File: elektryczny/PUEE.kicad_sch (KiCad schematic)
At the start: 9 parts, among them U1 ESP-12, U2 LM2596S-3.3

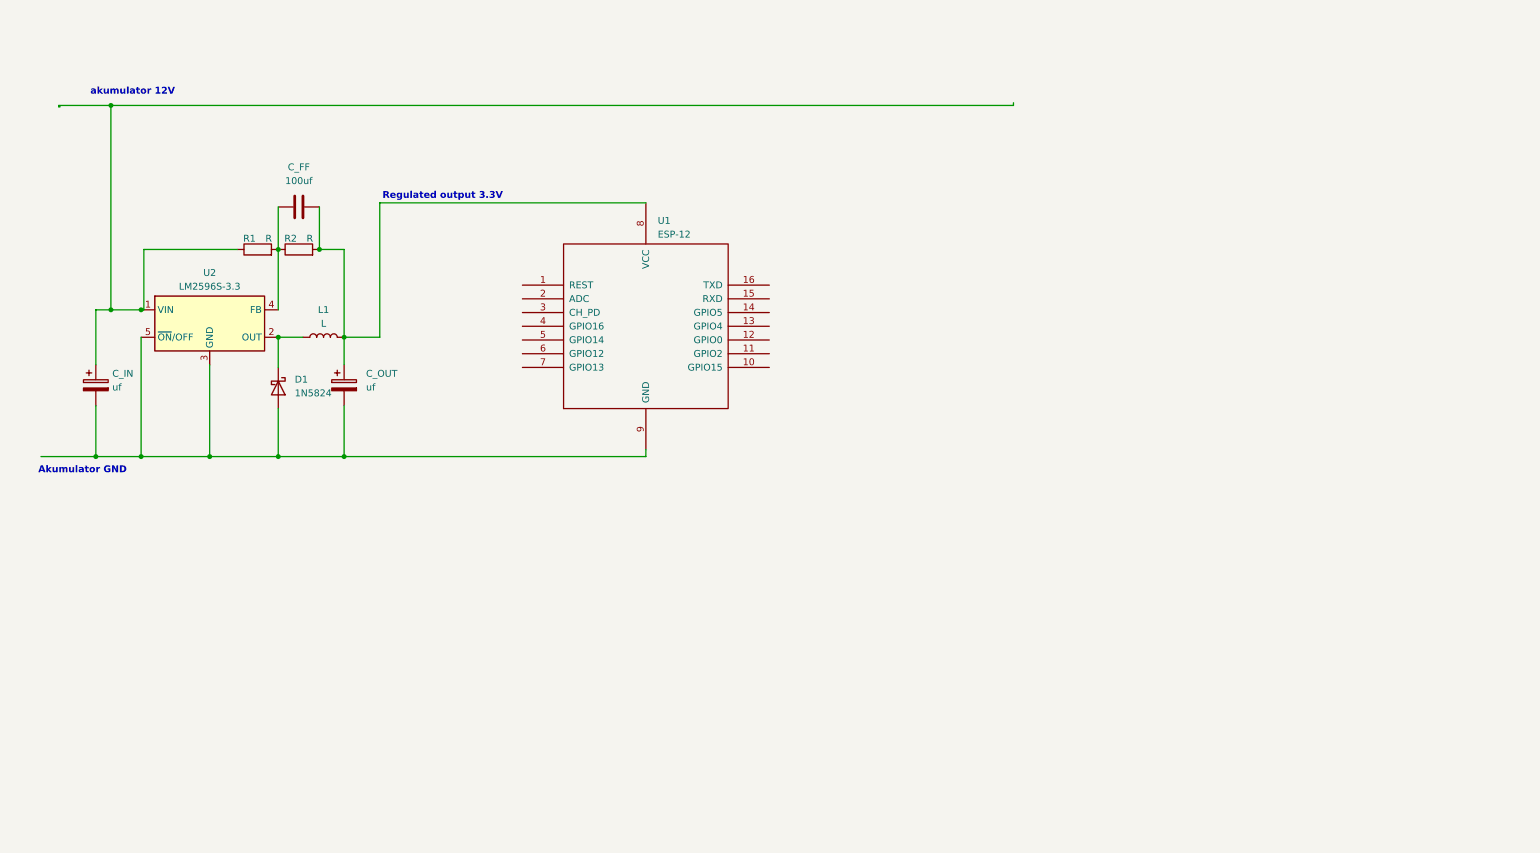
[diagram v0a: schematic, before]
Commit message: TJA1050 added
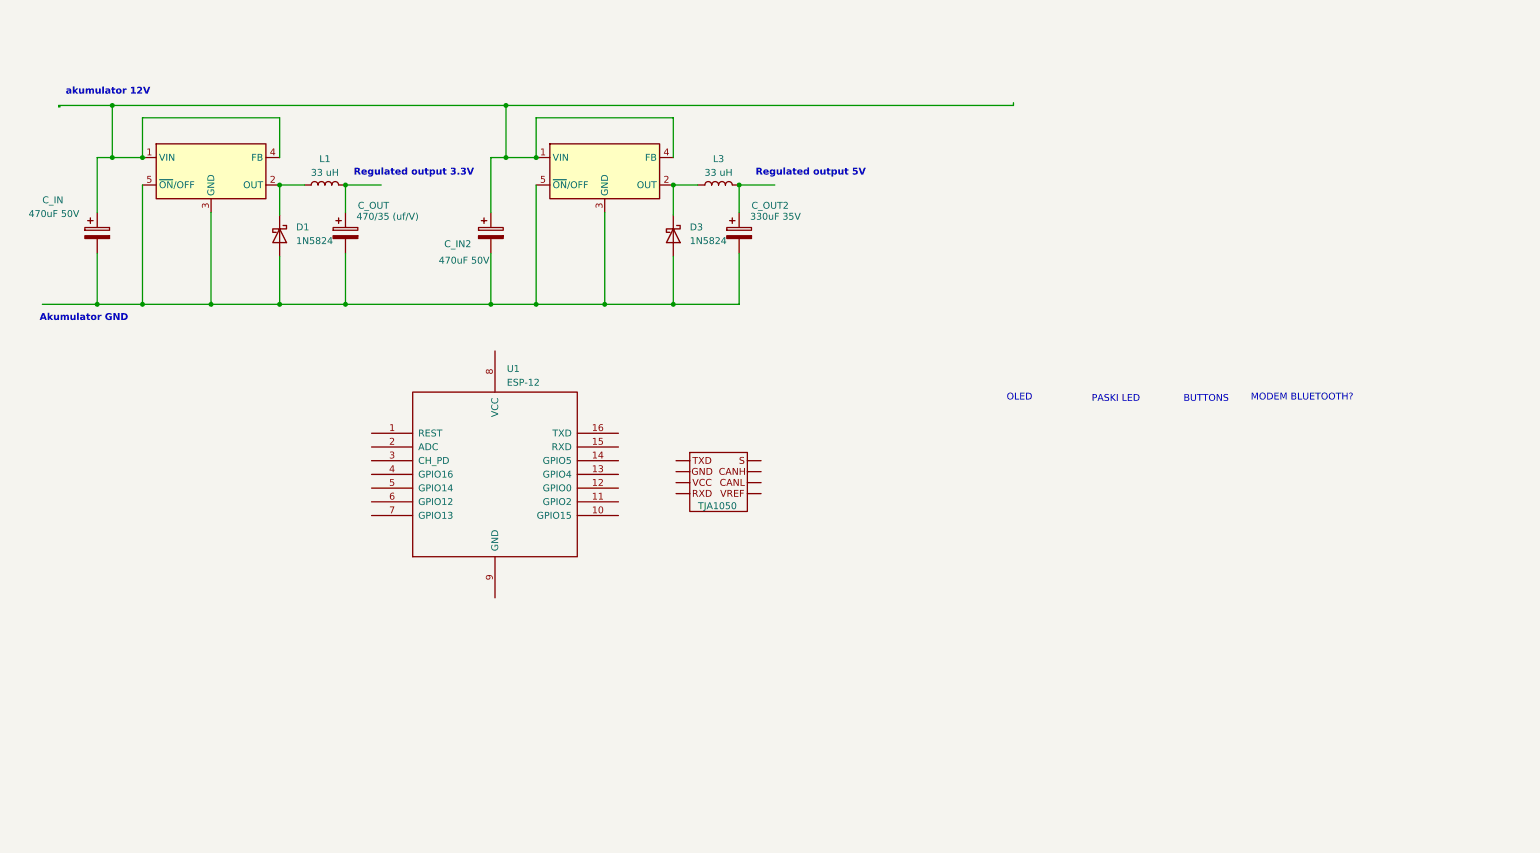
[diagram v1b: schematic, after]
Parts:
- removed C_FF: 100uf, symbol Device:C
- removed R1, R2: R, symbol Device:R
- added C_IN2: 470uF 50V, symbol Device:C_Polarized
- added C_OUT2: 330uF 35V, symbol Device:C_Polarized
- added D3: 1N5824, symbol Device:D_Schottky
- added L3: 33 uH, symbol Device:L
- added TJA1050: ~, symbol CAN:TJA1050
- added U4: LM2596, Package_TO_SOT_SMD:TO-263-5_TabPin3, symbol Regulator_Switching:LM2596S-3.3
- C_IN: value uf -> 470uF 50V
- C_OUT: value uf -> 470/35 (uf/V)
- L1: value L -> 33 uH
- U2: value LM2596S-3.3 -> LM2596
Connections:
- net at C_OUT.1, L1.2: no longer U1.8 (VCC)
- net at C_IN.2, C_OUT.2, D1.2 (A)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: now also C_IN2.2, C_OUT2.2, D3.2 (A), U4.3 (GND), U4.5 (~{ON}/OFF); no longer U1.9 (GND)
- net at U2.4 (FB): now also C_IN.1, U2.1 (VIN), C_IN2.1, U4.1 (VIN), U4.4 (FB)
- new net: D3.1 (K), L3.1, U4.2 (OUT)
- new net: C_OUT2.1, L3.2
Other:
- note added: "BUTTONS"
- note added: "MODEM BLUETOOTH?"
- note added: "OLED"
- note added: "PASKI LED"
- note added: "Regulated output 5V"
- moved on the sheet: C_IN, C_OUT, D1, L1, U1

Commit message: Wstępny schemat elektroniczny
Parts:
- removed TJA1050: ~, symbol CAN:TJA1050
- added Brd1: SSD1306, symbol SSD1306-128x64_OLED:SSD1306
- added C1, C2: 10nF, symbol Device:C
- added D2: LED_R, symbol Device:LED
- added Q1: 2N7000, Package_TO_SOT_THT:TO-92_Inline, symbol Transistor_FET:2N7000
- added R1, R3: 1K, symbol Device:R
- added R2, R4, R5: 10k, symbol Device:R
- added R6: 100, symbol Device:R
- added R7: 0000, symbol Device:R
- added SW1, SW2: SW_Push, symbol Switch:SW_Push
- added U3: SN65HVD230, Package_SO:SOIC-8_3.9x4.9mm_P1.27mm, symbol Interface_CAN_LIN:SN65HVD230
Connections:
- net at U1.13 (GPIO4): now also Brd1.4 (SDA)
- net at U1.14 (GPIO5): now also Brd1.3 (SCL)
- net at U1.15 (RXD): now also U3.4 (R)
- net at U1.16 (TXD): now also U3.1 (D)
- net at U1.8 (VCC): now also C_OUT.1, L1.2, Brd1.2 (VCC), U3.3 (VCC)
- net at U1.9 (GND): now also C_IN.2, C_OUT.2, D1.2 (A), U2.3 (GND), U2.5 (~{ON}/OFF), Brd1.1 (GND), R2.2, R4.2, U3.2 (GND), U3.8 (Rs)
- net at C_IN2.2, C_OUT2.2, D3.2 (A)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: no longer C_IN.2, C_OUT.2, D1.2 (A), U2.3 (GND), U2.5 (~{ON}/OFF)
- net at C_IN.1, U2.1 (VIN), U2.4 (FB): no longer C_IN2.1, U4.1 (VIN), U4.4 (FB)
- new net: Q1.2 (G), R5.1, R6.2
- new net: R1.2, R2.1, SW1.2
- new net: D2.1 (K), Q1.3 (D)
- new net: R3.2, R4.1, SW2.2
- new net: D2.2 (A), R7.1
- new net: C_IN2.1, U4.1 (VIN), U4.4 (FB)
- new net +3.3V: C1.1, C2.1, R7.2, SW1.1, SW2.1
- new net GND: Q1.1 (S), R5.2
- new net GPIO13: C1.2, R1.1, R6.1
- new net GPIO14: C2.2, R3.1
- no-connect marks 0 -> 1
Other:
- note added: "LINIA CAN"
- note removed: "MODEM BLUETOOTH?"
- moved on the sheet: C_IN2, C_OUT2, D3, L3, U1

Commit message: glowny schemat + MCU WIFI PSU Components
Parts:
- removed C_IN, C_IN2: 470uF 50V, symbol Device:C_Polarized
- removed C_OUT: 470/35 (uf/V), symbol Device:C_Polarized
- removed C_OUT2: 330uF 35V, symbol Device:C_Polarized
- removed D1, D3: 1N5824, symbol Device:D_Schottky
- removed D2: LED_R, symbol Device:LED
- removed L3: 33 uH, symbol Device:L
- removed Q1: 2N7000, Package_TO_SOT_THT:TO-92_Inline, symbol Transistor_FET:2N7000
- removed U1: ESP-12, symbol ESP8266:ESP-12
- removed U2, U4: LM2596, Package_TO_SOT_SMD:TO-263-5_TabPin3, symbol Regulator_Switching:LM2596S-3.3
- removed U3: SN65HVD230, Package_SO:SOIC-8_3.9x4.9mm_P1.27mm, symbol Interface_CAN_LIN:SN65HVD230
- added C10: 1uF, symbol Device:C
- added C11: 10uF, symbol Device:C
- added C12, C3, C4, C5, C8, CBoot, Cff, Cout: 100nF, symbol Device:C
- added C13, C14: 10nF, symbol Device:C
- added C6, C7: 20pF, symbol Device:C
- added C9: 4.7uF, symbol Device:C
- added R10, R9, Rfbb: 10k, symbol Device:R
- added R8: 1K, symbol Device:R
- added Rfbt: 30.9k, symbol Device:R
- added U1: STM32F042F4Px, Package_SO:TSSOP-20_4.4x6.5mm_P0.65mm, symbol MCU_ST_STM32F0:STM32F042F4Px
- added U2: ESP-12E, RF_Module:ESP-12E, symbol RF_Module:ESP-12E
- added U3: TPS562202DRLR, DRL0006A, symbol 2024-11-03_12-25-55:TPS562202DRLR
- added Y2: ABL-8MHZ-B2, Crystal:Crystal_HC49-U_Vertical, symbol Device:Crystal
- C1: value 10nF -> 4.7uF
- C2: value 10nF -> 100nF
- L1: value 33 uH -> 3.3 uH
- R1: value 1K -> 390
- R3: value 1K -> 10k
- R6: value 100 -> 10k
- R7: value 0000 -> 1K
- SW1: value SW_Push -> Button2
- SW2: value SW_Push -> Button1
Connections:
- net GND is gone; now on net -12V: R5.2
- net GPIO14 is gone; now on net -12V: C2.2, R3.1
- net -12V: now reaches Brd1.1 (GND), R4.2
- net -12V: now also Brd1.2 (VCC), C1.1, C1.2, C2.1, L1.2, R2.1, R6.1, SW1.2, SW2.1, C10.1, C10.2, C11.2, C12.2, C13.1, C14.1, C3.2, C4.2, C5.2, C8.1, C9.1, C9.2, Cff.1, Cout.1, Cout.2, R10.1, R9.1, Rfbb.1, Rfbt.2, U1.15 (VSSA), U1.16 (VDD), U2.15 (GND), U2.8 (VCC), U3.3 (GND); no longer R2.2
- net SPI1_SCK: now reaches Brd1.3 (SCL)
- net SPI1_SCK: now also U1.11 (PA5)
- net SPI1_MOSI: now reaches Brd1.4 (SDA)
- net SPI1_MOSI: now also U1.13 (PA7)
- net at R5.1: now also U2.17 (GPIO2); no longer R6.2
- net at R7.1: now also SW1.1, R9.2
- net at L1.1: now also CBoot.2, U3.2 (SW)
- removed net +3.3V: C1.1, C2.1, R7.2, SW1.1, SW2.1
- removed net GPIO13: C1.2, R1.1, R6.1
- new net: Cff.2, Rfbb.2, Rfbt.1, U3.6 (FB)
- new net: CBoot.1, U3.4 (BST)
- new net: R10.2, R8.2, SW2.2
- new net: C6.1, R1.1, Y2.1
- new net: R1.2, U1.3 (PF1)
- new net: R6.2, U2.16 (GPIO15)
- new net: C8.2, R2.2, U2.1 (~{RST})
- new net: R4.1, U2.18 (GPIO0)
- new net: R3.2, U2.3 (EN)
- new net: C7.1, U1.2 (PF0), Y2.2
- new net +12V: C11.1, C12.1, U3.1 (VIN), U3.5 (EN)
- new net GPIO_Button1: C14.2, R8.1, U1.6 (PA0)
- new net GPIO_Button2: C13.2, R7.2, U1.10 (PA4)
- new net GPIO_LED_Relay: U1.14 (PB1)
- new net NRST: C5.1, U1.4 (NRST)
- new net SWCLK: U1.20 (PA14)
- new net SWDIO: U1.19 (PA13)
- new net TIM2_CH2_PWM: U1.7 (PA1)
- new net USART1_RX: U1.18 (PA10/PA12), U2.22 (GPIO1/TXD)
- new net USART1_TX: U1.17 (PA9/PA11), U2.21 (GPIO3/RXD)
- new net USART2_RX: U1.9 (PA3)
- new net USART2_TX: U1.8 (PA2)
- new net VDDA: C3.1, C4.1, U1.5 (VDDA)
- no-connect marks 1 -> 15
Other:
- note added: "Connectors"
- note added: "LED strip"
- note added: "MCU"
- note added: "PSU"
- note added: "WIFI-module"
- note added: "buttons"
- note added: "components"
- note added: "display"
- note removed: "Akumulator GND"
- note removed: "BUTTONS"
- note removed: "LINIA CAN"
- note removed: "OLED"
- note removed: "PASKI LED"
- note removed: "Regulated output 3.3V"
- note removed: "Regulated output 5V"
- note removed: "akumulator 12V"

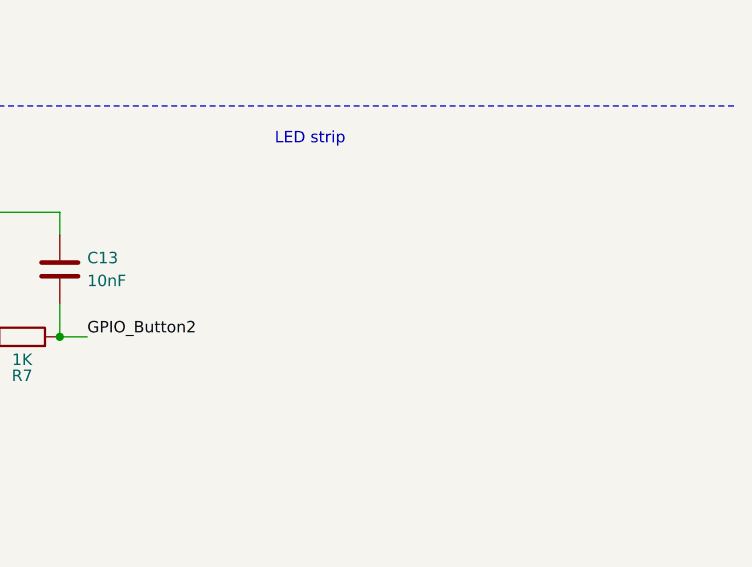
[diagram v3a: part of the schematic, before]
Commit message: Import symbolu LED
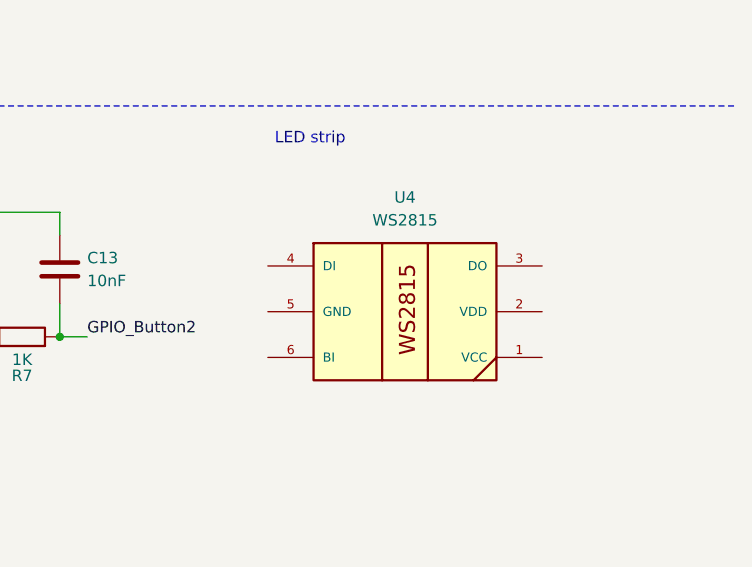
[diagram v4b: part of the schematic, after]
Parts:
- added U4: WS2815, WS2815:LED-TRICOLOR-5050, symbol WS2815:WS2815

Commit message: full schematic + blueprints
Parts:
- removed CBoot, Cff, Cout: 100nF, symbol Device:C
- removed Rfbb: 10k, symbol Device:R
- removed Rfbt: 30.9k, symbol Device:R
- removed U3: TPS562202DRLR, DRL0006A, symbol 2024-11-03_12-25-55:TPS562202DRLR
- removed U4: WS2815, WS2815:LED-TRICOLOR-5050, symbol WS2815:WS2815
- added C15, C16, C17, C18, C19, C20, C21, C22: 1uF, Capacitor_SMD:C_0805_2012Metric, symbol Device:C
- added C23: 47uF, Capacitor_SMD:C_0603_1608Metric, symbol Device:C
- added J1: CAN, Connector_Phoenix_MC:PhoenixContact_MCV_1,5_2-G-3.5_1x02_P3.50mm_Vertical, symbol Connector:Screw_Terminal_01x02
- added J2: LED2, Connector_PinHeader_2.54mm:PinHeader_1x03_P2.54mm_Vertical, symbol Connector_Generic:Conn_01x03
- added J3: OLED, Connector_PinHeader_2.54mm:PinHeader_1x04_P2.54mm_Vertical, symbol Connector_Generic:Conn_01x04
- added J4, J6: Button1, Connector_PinHeader_2.54mm:PinHeader_1x03_P2.54mm_Vertical, symbol Connector_Generic:Conn_01x03
- added J5: LED1, Connector_PinHeader_2.54mm:PinHeader_1x03_P2.54mm_Vertical, symbol Connector_Generic:Conn_01x03
- added J7: Conn_01x05, Connector_PinHeader_2.54mm:PinHeader_1x05_P2.54mm_Vertical, symbol Connector_Generic:Conn_01x05
- added R11: 120, Resistor_SMD:R_0805_2012Metric, symbol Device:R
- added R12: 100k, Resistor_SMD:R_0805_2012Metric, symbol Device:R
- added R13: 22k, Resistor_SMD:R_0805_2012Metric, symbol Device:R
- added U10, U11, U4, U5, U6, U7, U8, U9: WS2815, WS2815:LED-TRICOLOR-5050, symbol WS2815_mini:WS2815
- added U13: SN65HVD230QDRG4Q1, Package_SO:SOIC-8_3.9x4.9mm_P1.27mm, symbol Interface_CAN_LIN:SN65HVD230
- added U3: TPS54302DDCR, TPS54302DDCR:SOT95P280X110-6N, symbol TPS54302DDCR:TPS54302DDCR
- Brd1: footprint (none) -> Display:Adafruit_SSD1306
- C1, C10, C13, C14, C2, C3, C4, C5, C6, C7, C8, C9: footprint (none) -> Capacitor_SMD:C_0805_2012Metric
- C11: footprint (none) -> Capacitor_SMD:C_1210_3225Metric; Catalogue_number (none) -> GRM32ER61C476KE15
- C12: footprint (none) -> Capacitor_SMD:C_0805_2012Metric; Catalogue_number (none) -> 08053C104KAT2A
- L1: value 3.3 uH -> 22uH; footprint (none) -> Inductor_SMD:L_12x12mm_H8mm; Catalogue_number (none) -> CDRH127/LD-220MC
- R1, R10, R2, R3, R4, R5, R6, R7, R8, R9: footprint (none) -> Resistor_SMD:R_0805_2012Metric
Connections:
- net +12V: now also J2.3 (Pin_3), J5.3 (Pin_3), U10.2 (VDD), U11.2 (VDD), U3.3 (VIN), U4.2 (VDD), U5.2 (VDD), U6.2 (VDD), U7.2 (VDD), U8.2 (VDD), U9.2 (VDD); no longer C12.1
- net -12V: now also C6.2, C7.2, C15.2, C16.2, C17.2, C18.2, C19.2, C20.2, C21.2, C22.2, C23.2, J2.2 (Pin_2), J3.1 (Pin_1), J4.2 (Pin_2), J5.2 (Pin_2), J6.2 (Pin_2), J7.2 (Pin_2), R13.2, U10.5 (GND), U11.5 (GND), U13.2 (GND), U13.5 (Vref), U13.8 (Rs), U3.1 (GND), U4.5 (GND), U5.5 (GND), U6.5 (GND), U7.5 (GND), U8.5 (GND), U9.5 (GND); no longer Brd1.2 (VCC), C1.1, C10.2, C12.2, C13.1, C14.1, C2.1, C9.2, L1.2, R2.1, R3.1, R4.2, R5.2, SW1.2, SW2.1, U1.16 (VDD), U2.8 (VCC)
- net GPIO_Button1: now also J4.1 (Pin_1)
- net GPIO_Button2: now also J6.1 (Pin_1)
- net NRST: now also J7.5 (Pin_5)
- net SPI1_MOSI: now also J3.3 (Pin_3)
- net SPI1_SCK: now also J3.4 (Pin_4)
- net SWCLK: now also J7.3 (Pin_3)
- net SWDIO: now also J7.4 (Pin_4)
- net USART2_RX: now also U13.1 (D)
- net USART2_TX: now also U13.4 (R)
- net at L1.1: now also C12.2, U3.2 (SW)
- net GPIO_LED_RELAY2: now reaches U1.12 (PA6)
- net GPIO_LED_RELAY2: now also J2.1 (Pin_1), U4.4 (DI)
- net GPIO_LED_Relay renamed GPIO_LED_RELAY1
- net GPIO_LED_RELAY1: now also J5.1 (Pin_1)
- net TIM2_CH2_PWM: no longer names the net of U1.7 (PA1)
- new net: C17.1, U6.1 (NC)
- new net: U6.3 (DO), U7.4 (DI)
- new net: U5.3 (DO), U6.4 (DI)
- new net: C21.1, U10.1 (NC)
- new net: C18.1, U7.1 (NC)
- new net: U7.3 (DO), U8.4 (DI)
- new net: C15.1, U4.1 (NC)
- new net: U4.3 (DO), U5.4 (DI)
- new net: U10.3 (DO), U11.4 (DI)
- new net: U10.4 (DI), U9.3 (DO)
- new net: R12.2, R13.1, U3.4 (FB)
- new net: C22.1, U11.1 (NC)
- new net: C12.1, U3.6 (BOOT)
- new net: C19.1, U8.1 (NC)
- new net: C16.1, U5.1 (NC)
- new net: C20.1, U9.1 (NC)
- new net: U8.3 (DO), U9.4 (DI)
- new net CAN_H: J1.2 (Pin_2), R11.1, U13.7 (CANH)
- new net CAN_L: J1.1 (Pin_1), R11.2, U13.6 (CANL)
- new net VDD: Brd1.2 (VCC), C1.1, C10.2, C13.1, C14.1, C2.1, C23.1, C9.2, J3.2 (Pin_2), J4.3 (Pin_3), J6.3 (Pin_3), J7.1 (Pin_1), L1.2, R12.1, R2.1, R3.1, R4.2, R5.2, SW1.2, SW2.1, U1.16 (VDD), U13.3 (VCC), U2.8 (VCC)
- no-connect marks 15 -> 25
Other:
- note added: "/GPIO_LED_RELAY 1"
- note added: "Buttons"
- note added: "CAN interface"
- note added: "OLED Display"
- note added: "TODO: -choose footprints for connectors"
- note added: "for ERC only"
- note removed: "PSU"
- note removed: "buttons"
- note removed: "components"
- note removed: "display"
- moved on the sheet: Brd1, C13, C14, R10, R7, R8, R9, SW1, SW2
